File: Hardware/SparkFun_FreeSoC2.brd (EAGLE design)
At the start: 116.8 x 53.3 mm, 110 parts, among them U1 CY8C5888AXI-LP096, U2 MIC5219 5V, U3 MIC5219 3.3V, U4 2A/20V, U7 CY8C5868LTI-LP039, Y1 32.768kHz

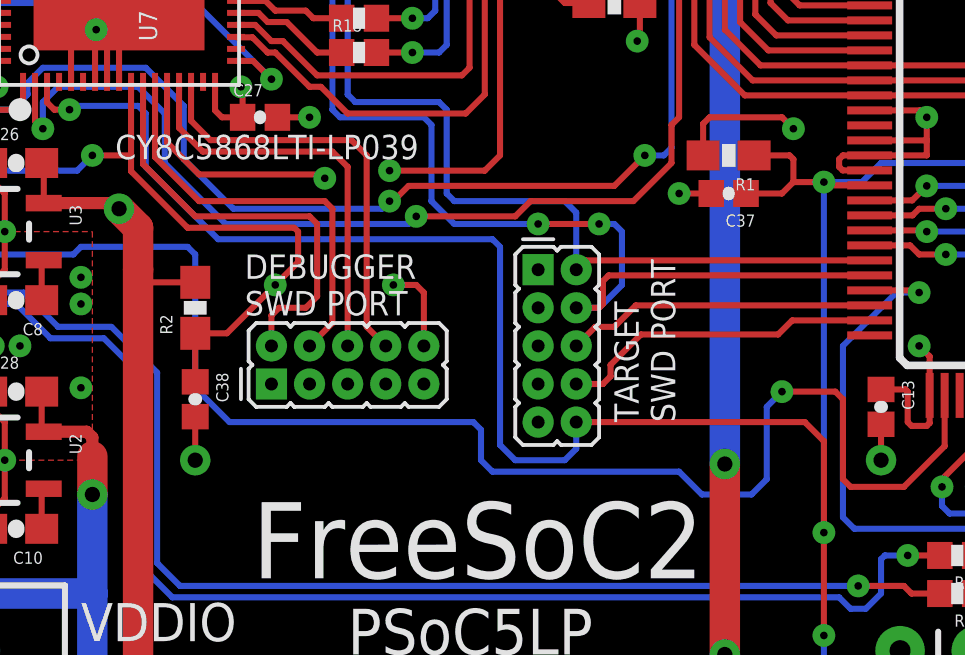
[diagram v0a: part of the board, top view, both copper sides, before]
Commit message: Rev to include changes from production
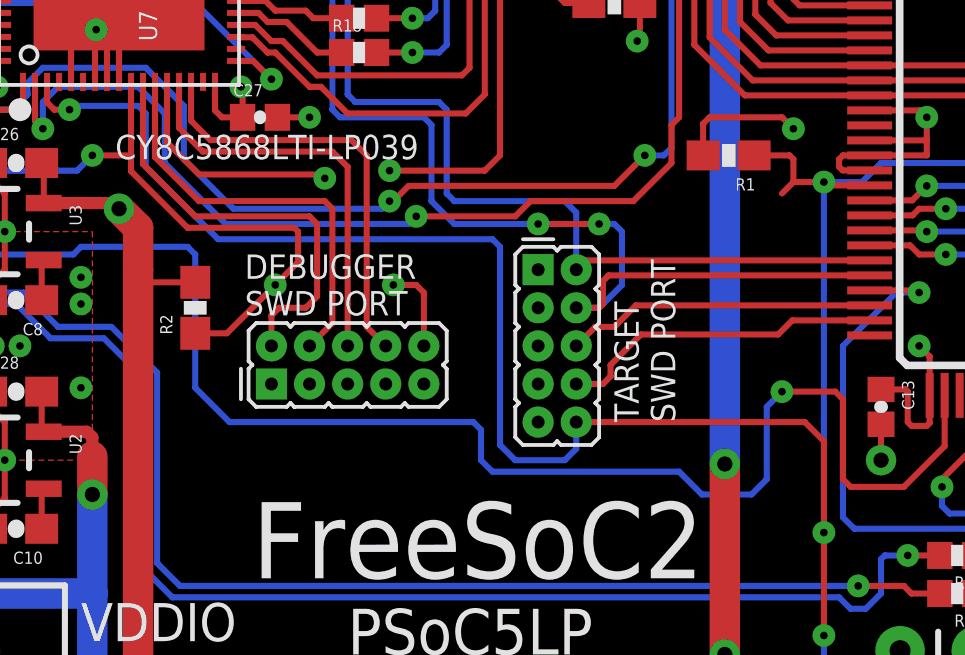
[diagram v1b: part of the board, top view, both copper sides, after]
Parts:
- removed C37, C38: 0.1uF, SparkFun-Capacitors:0402-CAP
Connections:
- net !DEBUG_RESET: no longer C38.1
- net !RESET: no longer C37.1
- net GND: no longer C37.2, C38.2
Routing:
- net GND: track 139.9 -> 137.4 mm, vias 49 -> 47
- net !DEBUG_RESET: track 46.1 -> 44.5 mm
- net !RESET: track 119.0 -> 117.8 mm
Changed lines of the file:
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@@
 <layer number="2" name="Route2" color="1" fill="3" visible="yes" active="yes"/>
 <layer number="15" name="Route15" color="4" fill="6" visible="yes" active="yes"/>
-<layer number="16" name="Bottom" color="1" fill="1" visible="yes" active="yes"/>
+<layer number="16" name="Bottom" color="1" fill="1" visible="no" active="yes"/>
 <layer number="17" name="Pads" color="2" fill="1" visible="yes" active="yes"/>
 <layer number="18" name="Vias" color="2" fill="1" visible="yes" active="yes"/>
@@
 <layer number="20" name="Dimension" color="15" fill="1" visible="yes" active="yes"/>
 <layer number="21" name="tPlace" color="16" fill="1" visible="yes" active="yes"/>
-<layer number="22" name="bPlace" color="14" fill="1" visible="yes" active="yes"/>
+<layer number="22" name="bPlace" color="14" fill="1" visible="no" active="yes"/>
 <layer number="23" name="tOrigins" color="15" fill="1" visible="yes" active="yes"/>
-<layer number="24" name="bOrigins" color="15" fill="1" visible="yes" active="yes"/>
-<layer number="25" name="tNames" color="7" fill="1" visible="yes" active="yes"/>
-<layer number="26" name="bNames" color="7" fill="1" visible="yes" active="yes"/>
-<layer number="27" name="tValues" color="7" fill="1" visible="yes" active="yes"/>
-<layer number="28" name="bValues" color="7" fill="1" visible="yes" active="yes"/>
-<layer number="29" name="tStop" color="7" fill="3" visible="yes" active="yes"/>
-<layer number="30" name="bStop" color="7" fill="6" visible="yes" active="yes"/>
-<layer number="31" name="tCream" color="7" fill="4" visible="yes" active="yes"/>
-<layer number="32" name="bCream" color="7" fill="5" visible="yes" active="yes"/>
-<layer number="39" name="tKeepout" color="4" fill="11" visible="yes" active="yes"/>
-<layer number="40" name="bKeepout" color="1" fill="11" visible="yes" active="yes"/>
-<layer number="41" name="tRestrict" color="4" fill="10" visible="yes" active="yes"/>
-<layer number="42" name="bRestrict" color="1" fill="10" visible="yes" active="yes"/>
-<layer number="43" name="vRestrict" color="2" fill="10" visible="yes" active="yes"/>
-<layer number="44" name="Drills" color="7" fill="1" visible="yes" active="yes"/>
-<layer number="45" name="Holes" color="7" fill="1" visible="yes" active="yes"/>
-<layer number="46" name="Milling" color="3" fill="1" visible="yes" active="yes"/>
-<layer number="47" name="Measures" color="7" fill="1" visible="yes" active="yes"/>
-<layer number="51" name="tDocu" color="6" fill="1" visible="yes" active="yes"/>
+<layer number="24" name="bOrigins" color="15" fill="1" visible="no" active="yes"/>
+<layer number="25" name="tNames" color="7" fill="1" visible="no" active="yes"/>
+<layer number="26" name="bNames" color="7" fill="1" visible="no" active="yes"/>
+<layer number="27" name="tValues" color="7" fill="1" visible="no" active="yes"/>
+<layer number="28" name="bValues" color="7" fill="1" visible="no" active="yes"/>
+<layer number="29" name="tStop" color="7" fill="3" visible="no" active="yes"/>
+<layer number="30" name="bStop" color="7" fill="6" visible="no" active="yes"/>
+<layer number="31" name="tCream" color="7" fill="4" visible="no" active="yes"/>
+<layer number="32" name="bCream" color="7" fill="5" visible="no" active="yes"/>
+<layer number="39" name="tKeepout" color="4" fill="11" visible="no" active="yes"/>
+<layer number="40" name="bKeepout" color="1" fill="11" visible="no" active="yes"/>
+<layer number="41" name="tRestrict" color="4" fill="10" visible="no" active="yes"/>
+<layer number="42" name="bRestrict" color="1" fill="10" visible="no" active="yes"/>
+<layer number="43" name="vRestrict" color="2" fill="10" visible="no" active="yes"/>
+<layer number="44" name="Drills" color="7" fill="1" visible="no" active="yes"/>
+<layer number="45" name="Holes" color="7" fill="1" visible="no" active="yes"/>
+<layer number="46" name="Milling" color="3" fill="1" visible="no" active="yes"/>
+<layer number="47" name="Measures" color="7" fill="1" visible="no" active="yes"/>
+<layer number="51" name="tDocu" color="6" fill="1" visible="no" active="yes"/>
 <layer number="52" name="bDocu" color="7" fill="1" visible="no" active="no"/>
 <layer number="3" name="Route3" color="4" fill="3" visible="no" active="no"/>
@@
 <attribute name="PROD_ID" value="RES-07857" x="48.26" y="26.67" size="1.778" layer="27" font="vector" ratio="15" rot="R180" display="off"/>
 </element>
-<element name="C37" library="SparkFun-Capacitors" package="0402-CAP" value="0.1uF" x="48.26" y="25.4" rot="R180">
-<attribute name="PROD_ID" value="CAP-12416" x="48.26" y="25.4" size="1.778" layer="27" font="vector" ratio="15" rot="R180" display="off"/>
-</element>
-<element name="C38" library="SparkFun-Capacitors" package="0402-CAP" value="0.1uF" x="30.48" y="18.542" rot="R270">
-<attribute name="PROD_ID" value="CAP-12416" x="30.48" y="18.542" size="1.778" layer="27" font="vector" ratio="15" rot="R270" display="off"/>
-</element>
 <element name="R2" library="SparkFun-Resistors" package="0603-RES" value="4.7K" x="30.48" y="21.59" rot="R90">
 <attribute name="PROD_ID" value="RES-07857" x="30.48" y="21.59" size="1.778" layer="27" font="vector" ratio="15" rot="R90" display="off"/>
@@
 <wire x1="21.772" y1="38.735" x2="21.772" y2="39.878" width="0.2032" layer="1"/>
 <contactref element="JP10" pad="1"/>
-<contactref element="C37" pad="2"/>
-<contactref element="C38" pad="2"/>
-<wire x1="30.48" y1="17.962" x2="30.48" y2="16.51" width="0.2032" layer="1"/>
-<via x="30.48" y="16.51" extent="1-16" drill="0.508"/>
 <contactref element="R6" pad="1"/>
 <contactref element="R5" pad="1"/>
@@
 <wire x1="20.36" y1="33.543" x2="20.375" y2="33.528" width="0.2032" layer="1"/>
 <wire x1="28.139" y1="40.132" x2="29.265" y2="40.132" width="0.2032" layer="1"/>
-<wire x1="47.68" y1="25.4" x2="46.609" y2="25.4" width="0.2032" layer="1"/>
-<via x="46.609" y="25.4" extent="1-16" drill="0.254"/>
 </signal>
 <signal name="N$13">
@@
 <wire x1="25.54" y1="28.435" x2="25.781" y2="28.194" width="0.2032" layer="1"/>
 <wire x1="25.781" y1="28.194" x2="26.289" y2="28.194" width="0.2032" layer="1"/>
-<contactref element="C37" pad="1"/>
 <contactref element="R1" pad="1"/>
-<wire x1="48.84" y1="25.4" x2="50.038" y2="25.4" width="0.2032" layer="1"/>
 <wire x1="50.038" y1="25.4" x2="50.419" y2="25.781" width="0.2032" layer="1"/>
 <wire x1="50.419" y1="25.781" x2="51.435" y2="25.781" width="0.2032" layer="1"/>
@@
 <wire x1="27.051" y1="26.67" x2="28.34" y2="26.67" width="0.2032" layer="1"/>
 <contactref element="R2" pad="1"/>
-<contactref element="C38" pad="1"/>
-<wire x1="30.48" y1="20.74" x2="30.48" y2="19.122" width="0.2032" layer="1"/>
 <wire x1="33.147" y1="22.352" x2="31.535" y2="20.74" width="0.2032" layer="1"/>
 <wire x1="30.48" y1="20.74" x2="31.535" y2="20.74" width="0.2032" layer="1"/>

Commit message: Revisions from first production run
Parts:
- C18, C24: value 22pF -> (none); device SparkFun-Capacitors:0603-CAP -> SparkFun-Capacitors:CAP-PTH-SMALL
- moved C24 1.42 mm to (75.6, 22.9), turned to 90 degrees
- moved C18 0.64 mm to (80.6, 22.9), turned to 90 degrees
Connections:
- net A4: now also JP7.9; no longer JP7.10
- net A5: now also JP7.10; no longer JP7.9
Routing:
- net GND: track 137.4 -> 130.6 mm, vias 47 -> 46
- net A4: track 86.0 -> 83.3 mm, vias 4 -> 5
- net A5: track 94.5 -> 97.2 mm
- net P12.2: track 56.8 -> 58.6 mm
- net P12.3: track 59.2 -> 60.6 mm
- net P15.3: track 11.0 -> 9.71 mm
- net P15.2: track 17.9 -> 16.6 mm
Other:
- board text added: "A4/SDA P6.1"
- board text added: "A5/SCL P6.0"
- board text added: "USB DEBUGGER"
- board text added: "USB TARGET"
- board text added: "v12"
- board text removed: "A4/SCL P6.1"
- board text removed: "A5/SDA P6.0"
- board text removed: "DEBUGGER"
- board text removed: "TARGET"
- board text removed: "v11"
